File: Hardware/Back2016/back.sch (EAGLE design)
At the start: 12 parts, among them J1 RASPBERRYPI-40-PIN-GPIO-SMT

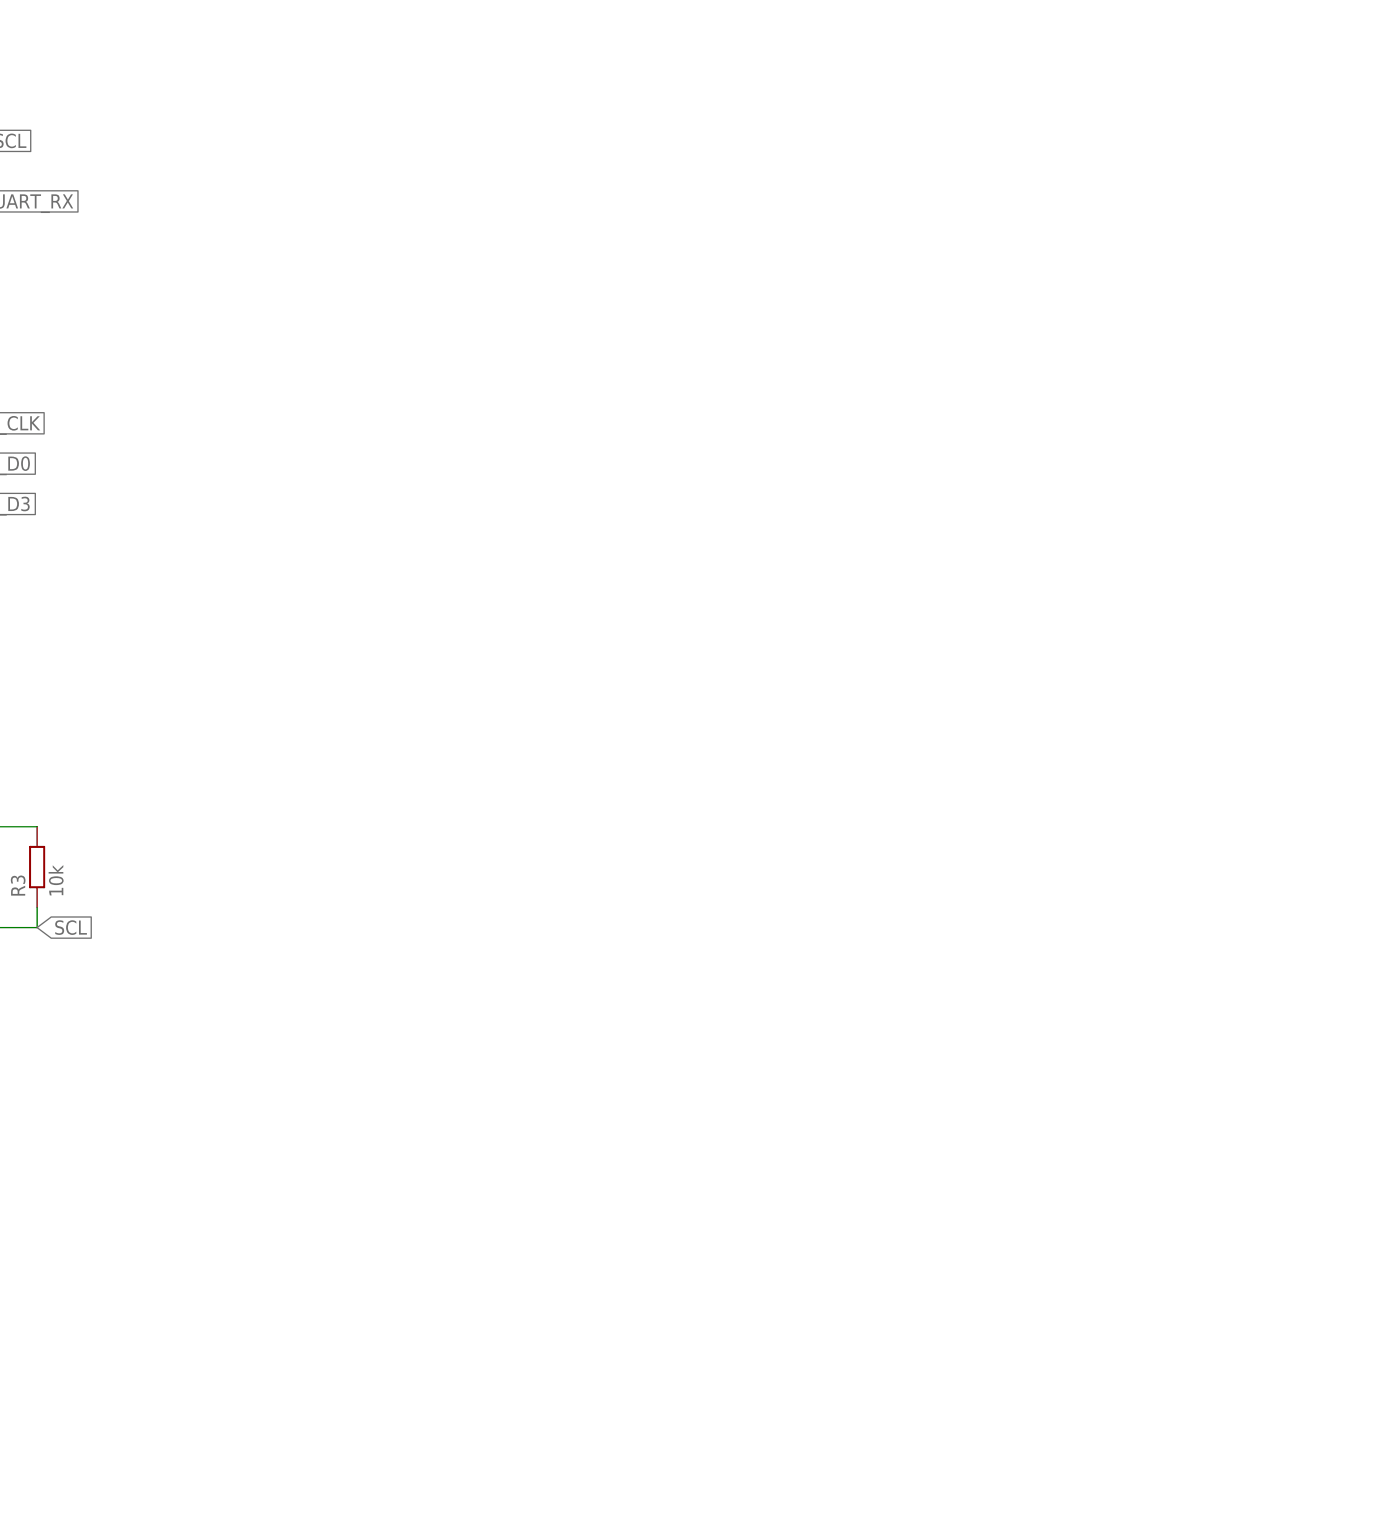
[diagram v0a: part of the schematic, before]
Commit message: Added Audio out
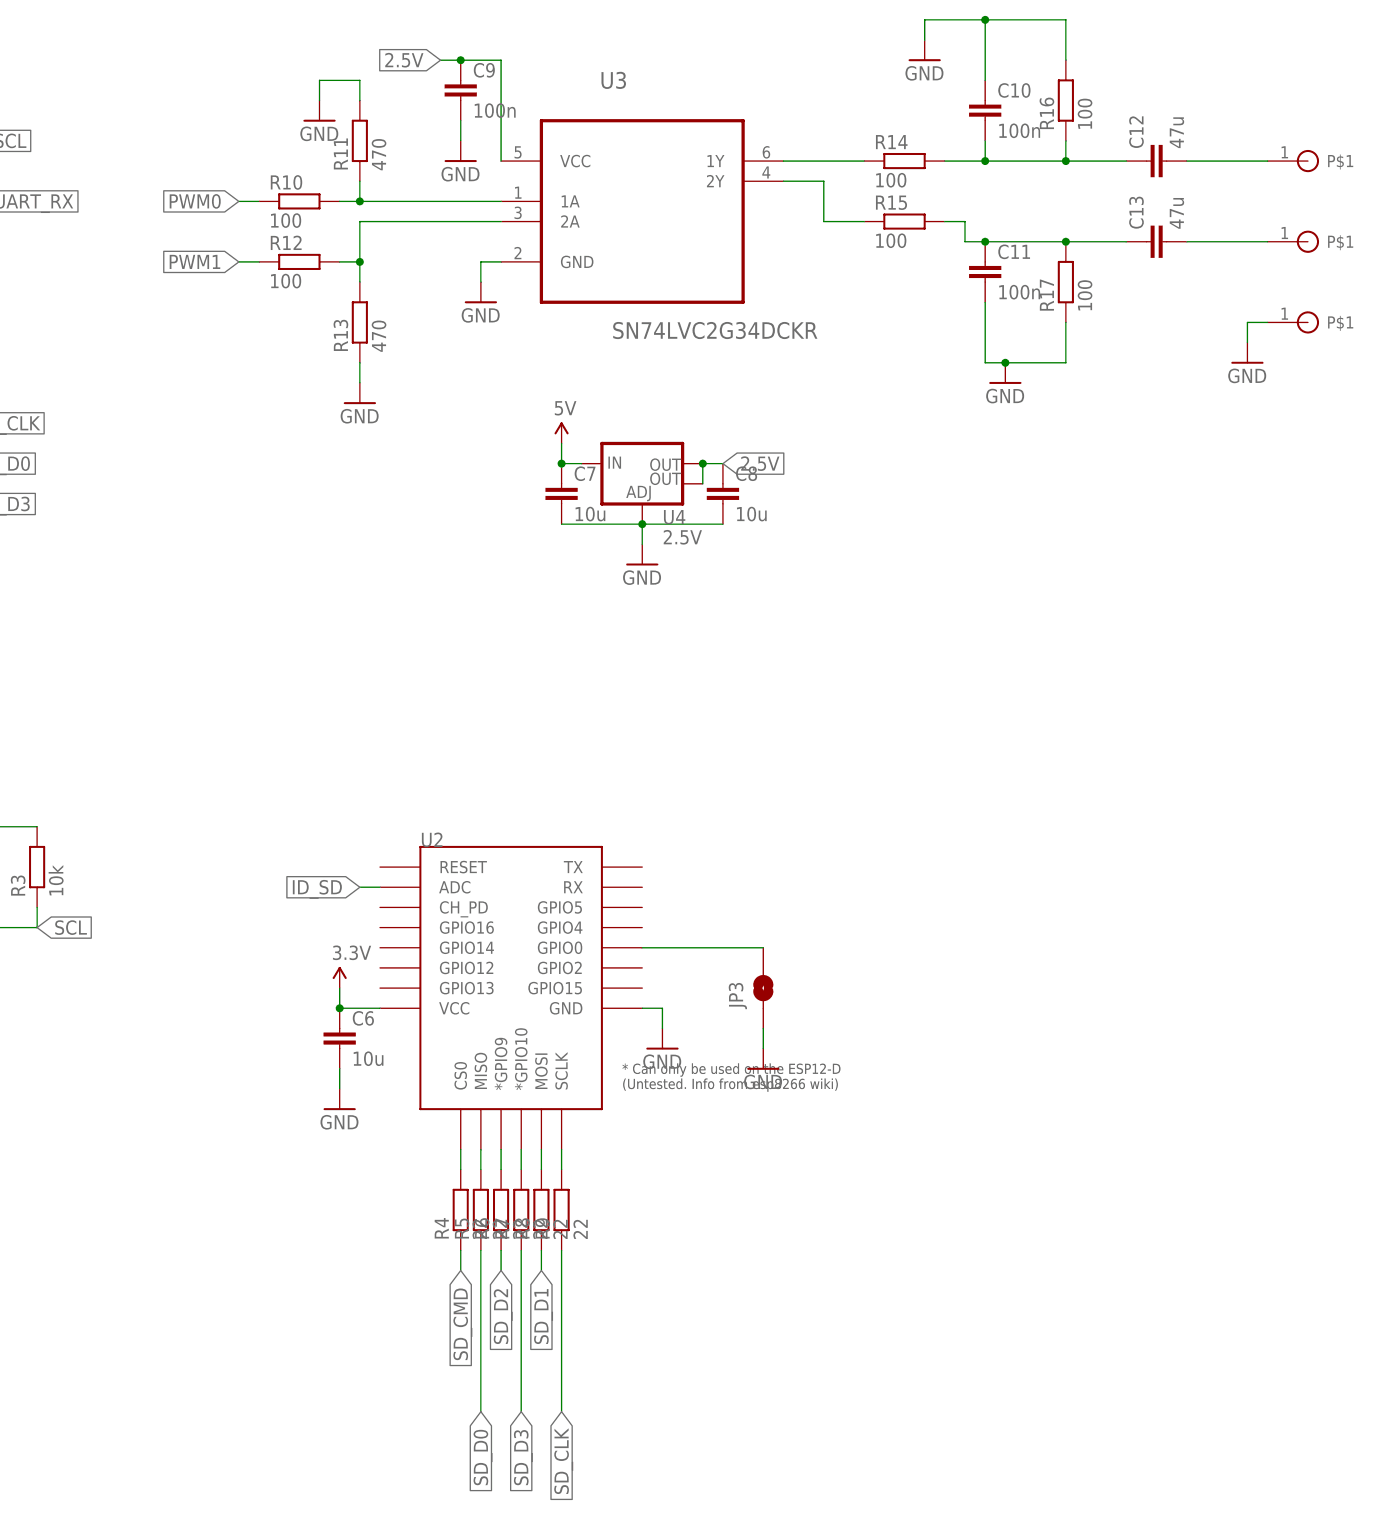
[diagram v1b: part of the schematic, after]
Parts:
- added C10, C11, C9: 100n, timearc:C-EUC0603
- added C12, C13: 47u, timearc:C-EUC0603
- added C6, C7, C8: 10u, timearc:C-EUC0603
- added JP3: JUMPER-PAD-2-NOROUND, SparkFun-Passives:JUMPER-PAD-2-NOROUND
- added R10, R12, R14, R15, R16, R17: 100, timearc:R-EU_R0603
- added R11, R13: 470, timearc:R-EU_R0603
- added R4, R5, R6, R7, R8, R9: 22, timearc:R-EU_R0603
- added U$1, U$2, U$3: SOLDER_PAD, timearc:SOLDER_PAD
- added U2: (no value), timearc:ESP12ESMD
- added U3: SN74LVC2G34DCKR, timearc:SN74LVC2G34DCKR
- added U4: 2.5V, SparkFun-PowerIC:V_REG_LM1117SOT223
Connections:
- new net 2.5V: C8.1, C9.1, U3.VCC, U4.OUT, U4.OUT@1
- new net N$10: R8.2, U2.MOSI
- new net N$11: R9.2, U2.SCLK
- new net N$12: JP3.2, U2.GPIO0
- new net N$13: R10.2, R11.1, U3.1A
- new net N$14: R12.2, R13.2, U3.2A
- new net N$15: R15.1, U3.2Y
- new net N$16: C10.2, C12.1, R14.2, R16.1
- new net N$17: C11.1, C13.1, R15.2, R17.2
- new net N$19: C12.2, U$1.P$1
- new net N$20: C13.2, U$2.P$1
- new net N$5: R14.1, U3.1Y
- new net N$6: R4.2, U2.CS0
- new net N$7: R5.2, U2.MISO
- new net N$8: R6.2, U2.*GPIO9
- new net N$9: R7.2, U2.*GPIO10
- net 3.3V: now also C6.1, U2.VCC
- net 5V: now also C7.1, U4.IN
- net GND: now also C10.1, C11.2, C6.2, C7.2, C8.2, C9.2, JP3.1, R11.2, R13.1, R16.2, R17.1, U$3.P$1, U2.GND, U3.GND, U4.ADJ
- net ID_SD: now also U2.ADC
- net PWM0: now also R10.1
- net PWM1: now also R12.1
- net SD_CLK: now also R9.1
- net SD_CMD: now also R4.1
- net SD_D0: now also R5.1
- net SD_D1: now also R8.1
- net SD_D2: now also R6.1
- net SD_D3: now also R7.1

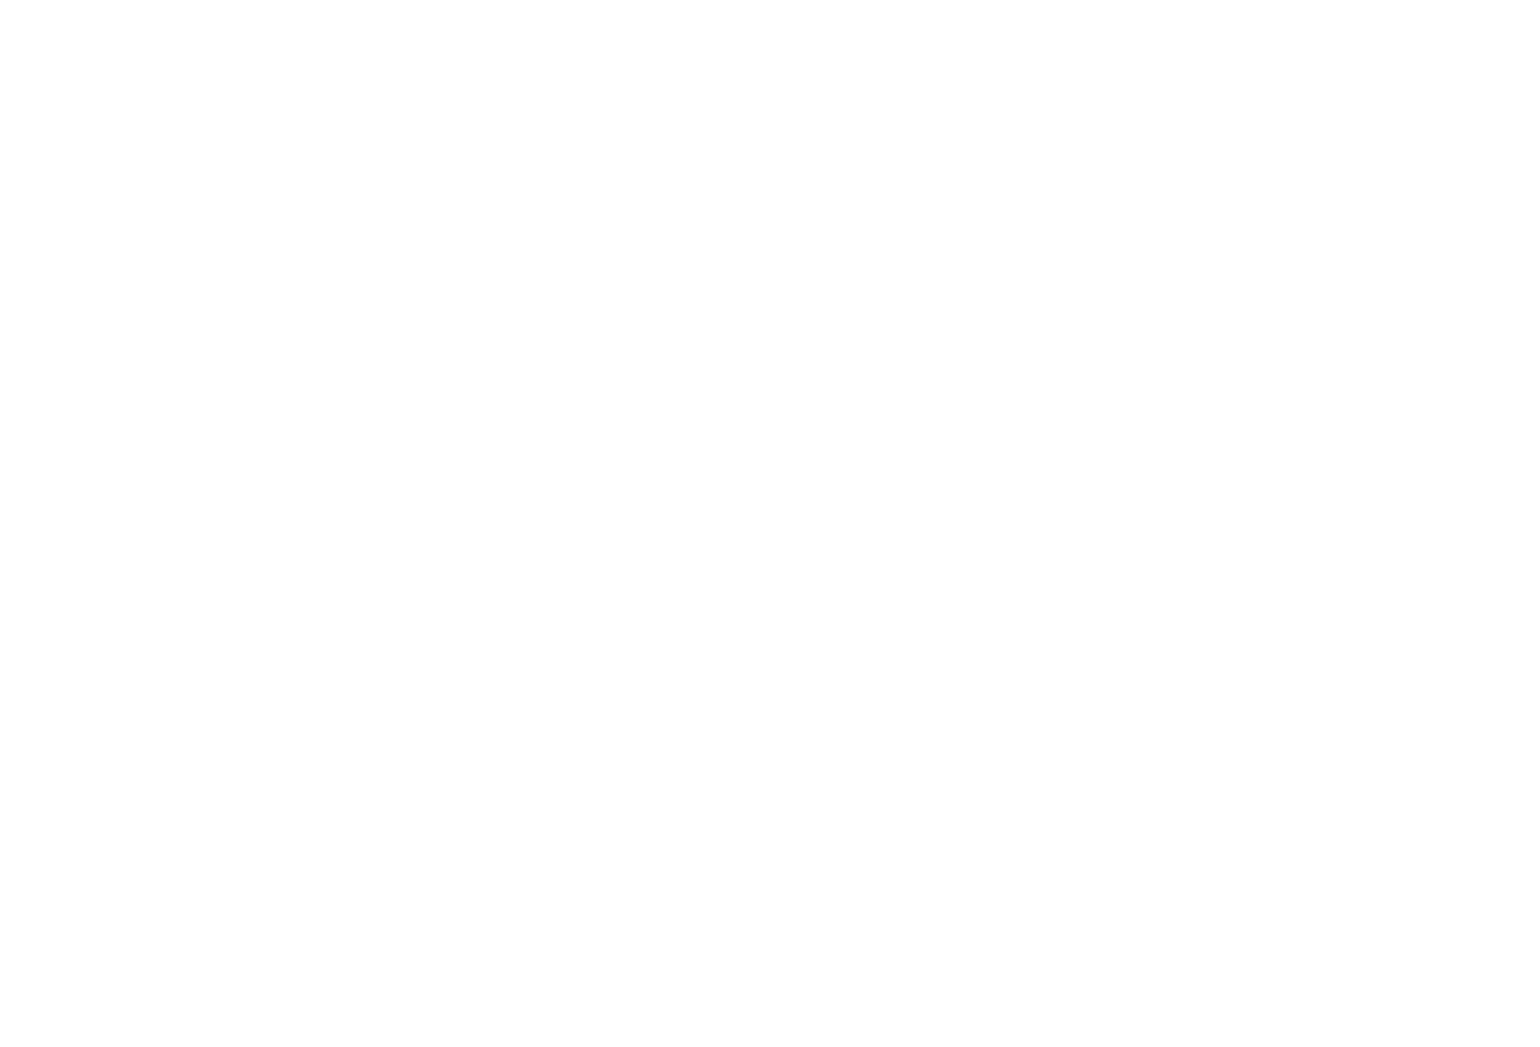
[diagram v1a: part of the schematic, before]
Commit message: Added Teensy LC SMD version
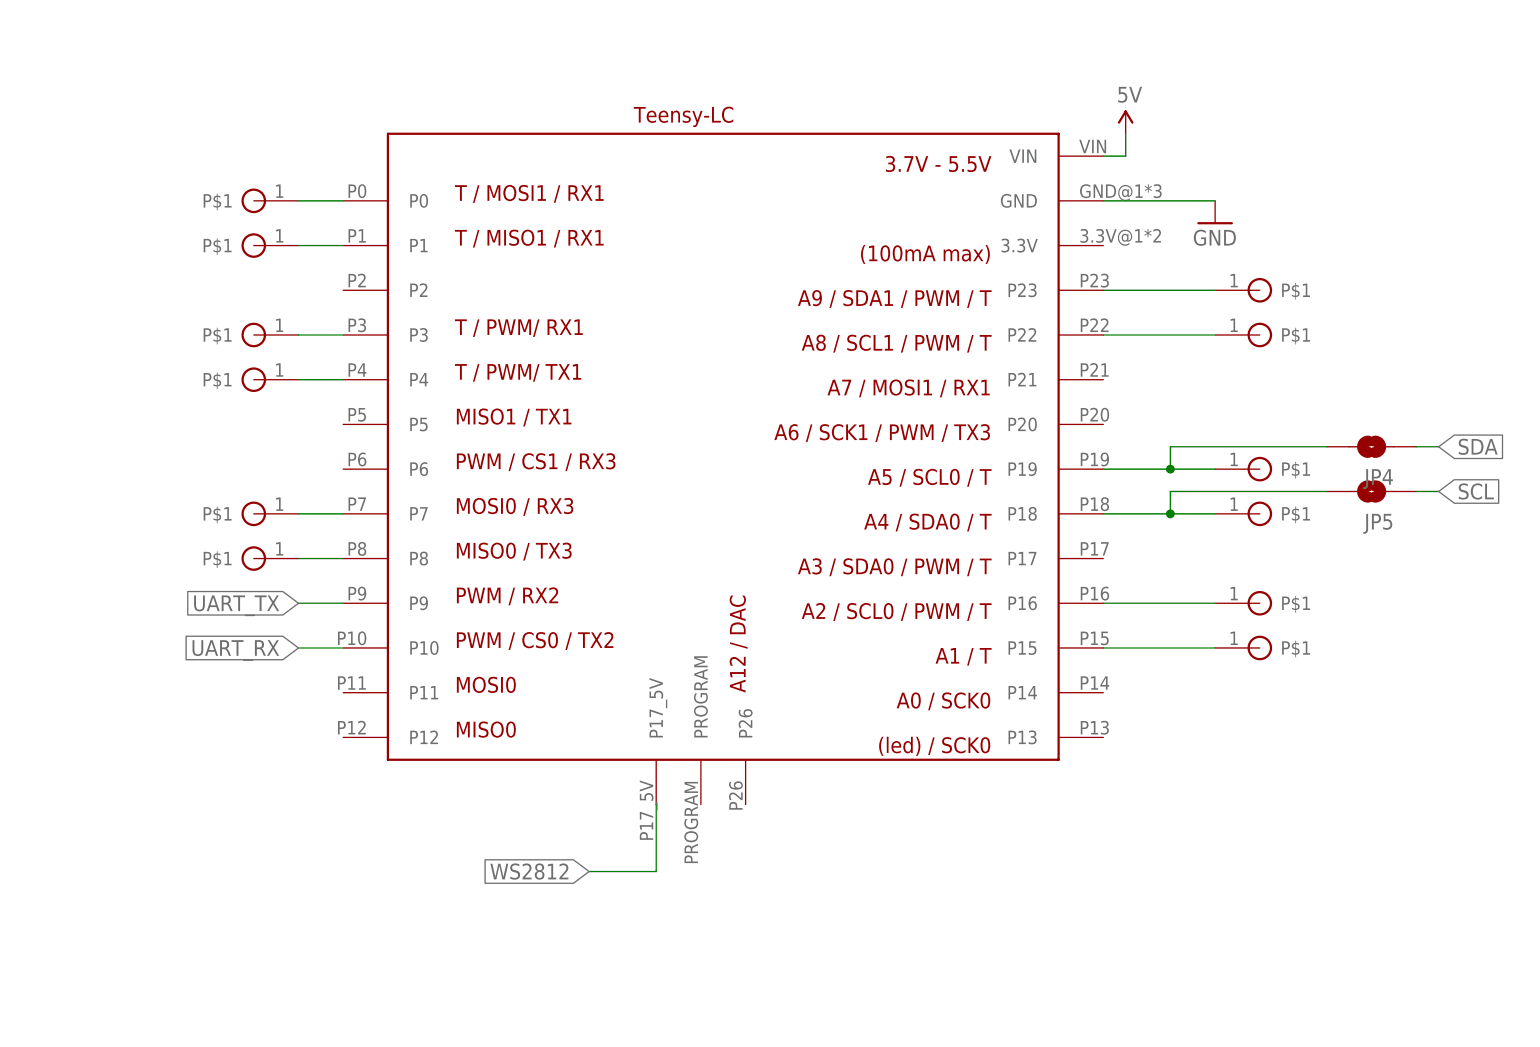
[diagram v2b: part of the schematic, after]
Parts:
- added JP4, JP5: JUMPER-PAD-2-NOYES_SILK, SparkFun-Passives:JUMPER-PAD-2-NOYES_SILK
- added RX3, TX3, U$10, U$11, U$12, U$13, U$14, U$5, U$6, U$7, U$8, U$9: SOLDER_PAD, timearc:SOLDER_PAD
- added U$4: TEENSY_LCSMD, timearc:TEENSY_LCSMD
- JP1, JP2, JP3: value JUMPER-PAD-2-NOROUND -> JUMPER-PAD-2-NOYES_SILK; device SparkFun-Passives:JUMPER-PAD-2-NOROUND -> SparkFun-Passives:JUMPER-PAD-2-NOYES_SILK
- U1: device SparkFun-Sensors:MPU-9150QFN-24-NP -> timearc:MPU-9150QFN-24-NP
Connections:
- new net N$21: U$4.P0, U$5.P$1
- new net N$22: U$4.P1, U$6.P$1
- new net N$23: U$4.P3, U$7.P$1
- new net N$24: U$4.P4, U$8.P$1
- new net N$25: U$4.P23, U$9.P$1
- new net N$26: U$10.P$1, U$4.P22
- new net N$27: JP4.2, U$11.P$1, U$4.P19
- new net N$28: JP5.2, U$12.P$1, U$4.P18
- new net N$29: U$13.P$1, U$4.P16
- new net N$30: U$14.P$1, U$4.P15
- new net N$31: RX3.P$1, U$4.P7
- new net N$32: TX3.P$1, U$4.P8
- new net WS2812: U$4.P17_5V
- net 5V: now also U$4.VIN
- net GND: now also U$4.GND
- net SCL: now also JP5.1
- net SDA: now also JP4.1
- net UART_RX: now also U$4.P10
- net UART_TX: now also U$4.P9

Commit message: Start routing board Back2016/back.brd Added keep out to Front2014/uac.brd Tweaked the 3d print design
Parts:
- removed R1: (no value), timearc:R-EU_R0603
- removed U$1, U$10, U$11, U$12, U$13, U$14, U$2, U$3, U$5, U$6, U$7, U$8, U$9: SOLDER_PAD, timearc:SOLDER_PAD
- added 5V_FRONT, 5V_POWER, 5V_WS1282, AUDIO_GND, AUDIO_L, AUDIO_R, DO_WS1282, GND_FRONT, GND_POWER, GND_T1_T2, GND_T3_T4, GND_T5_T6, GND_T7_T8, GND_T_SPARE, GND_WS2812, SCL/TOUCH, SDA/TOUCH, TOUCH1, TOUCH2, TOUCH3, TOUCH4, TOUCH5, TOUCH6, TOUCH7, TOUCH8: SOLDER_PAD, timearc:SOLDER_PAD
- added LED1, LED10, LED11, LED12, LED2, LED3, LED4, LED5, LED6, LED7, LED8, LED9: WS2812B5050, adafruit:WS2812B5050
- C1: value (none) -> 10u; device timearc:C-EUC0603 -> timearc:C-EUC0805
- C12, C13, C6, C7, C8: device timearc:C-EUC0603 -> timearc:C-EUC0805
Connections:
- new net N$18: LED1.DO, LED2.DI
- new net N$33: LED2.DO, LED3.DI
- new net N$34: LED3.DO, LED4.DI
- new net N$35: LED4.DO, LED5.DI
- new net N$36: LED5.DO, LED6.DI
- new net N$37: LED6.DO, LED7.DI
- new net N$38: LED7.DO, LED8.DI
- new net N$39: LED8.DO, LED9.DI
- new net N$40: LED10.DI, LED9.DO
- new net N$41: LED10.DO, LED11.DI
- new net N$42: LED11.DO, LED12.DI
- new net N$43: DO_WS1282.P$1, LED12.DO
- net 5V: now also 5V_FRONT.P$1, 5V_POWER.P$1, 5V_WS1282.P$1, C1.1, LED1.VDD, LED10.VDD, LED11.VDD, LED12.VDD, LED2.VDD, LED3.VDD, LED4.VDD, LED5.VDD, LED6.VDD, LED7.VDD, LED8.VDD, LED9.VDD
- net GND: now also AUDIO_GND.P$1, C1.2, GND_FRONT.P$1, GND_POWER.P$1, GND_T1_T2.P$1, GND_T3_T4.P$1, GND_T5_T6.P$1, GND_T7_T8.P$1, GND_T_SPARE.P$1, GND_WS2812.P$1, LED1.GND, LED10.GND, LED11.GND, LED12.GND, LED2.GND, LED3.GND, LED4.GND, LED5.GND, LED6.GND, LED7.GND, LED8.GND, LED9.GND; no longer U$3.P$1
- net N$19: now also AUDIO_L.P$1; no longer U$1.P$1
- net N$20: now also AUDIO_R.P$1; no longer U$2.P$1
- net N$21: now also TOUCH1.P$1; no longer U$5.P$1
- net N$22: now also TOUCH2.P$1; no longer U$6.P$1
- net N$23: now also TOUCH3.P$1; no longer U$7.P$1
- net N$24: now also TOUCH4.P$1; no longer U$8.P$1
- net N$25: now also TOUCH5.P$1; no longer U$9.P$1
- net N$26: now also TOUCH6.P$1; no longer U$10.P$1
- net N$27: now also SDA/TOUCH.P$1; no longer U$11.P$1
- net N$28: now also SCL/TOUCH.P$1; no longer U$12.P$1
- net N$29: now also TOUCH7.P$1; no longer U$13.P$1
- net N$30: now also TOUCH8.P$1; no longer U$14.P$1
- net PWM0: now also R12.1; no longer R10.1
- net PWM1: now also R10.1; no longer R12.1
- net WS2812: now also LED1.DI
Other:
- moved on the sheet: C1, C10, C11, C12, C13, C2, C3, C4, C5, C6, C7, C8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

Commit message: 100% connected
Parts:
- added C14, C15: 10u, timearc:C-EUC0805
- added JP6, JP7: JUMPER-PAD-2-NOYES_SILK, SparkFun-Passives:JUMPER-PAD-2-NOYES_SILK
- added U5: 3.3V, SparkFun-PowerIC:V_REG_LM1117SOT223
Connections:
- new net 3.3V_RPI: J1.3.3V@1, J1.3.3V@17, JP7.1
- new net N$44: C15.1, JP6.1, U5.OUT, U5.OUT@1
- net 3.3V: now also JP6.2, JP7.2; no longer J1.3.3V@1, J1.3.3V@17
- net 5V: now also C14.1, U5.IN
- net GND: now also C14.2, C15.2, U5.ADJ
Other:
- moved on the sheet: C1, C7, C8, U4
